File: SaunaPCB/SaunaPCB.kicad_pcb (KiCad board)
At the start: 2 copper layers, 200 x 110 mm, 61 parts, among them J201 KL3RM7.62, J202 KL3RM7.62, J203 KL3RM7.62, J204 KL2RM5.08, J205 KL3RM7.62, J206 KL3RM7.62, J301 KL2RM5.08, J302 KL2RM5.08, J303 KL2RM5.08, K201 Relais_SPDT_CO, K202 Relais_SPDT_CO, K203 Relais_SPDT_CO, K204 Relais_SPDT_CO, K205 Relais_SPDT_CO, K206 Relais_SPDT_CO, K207 Relais_SPDT_CO, U201 LHE05-20B24, U202 4N25, U203 4N25, U204 4N25, U301 ESP32-DEVKITC

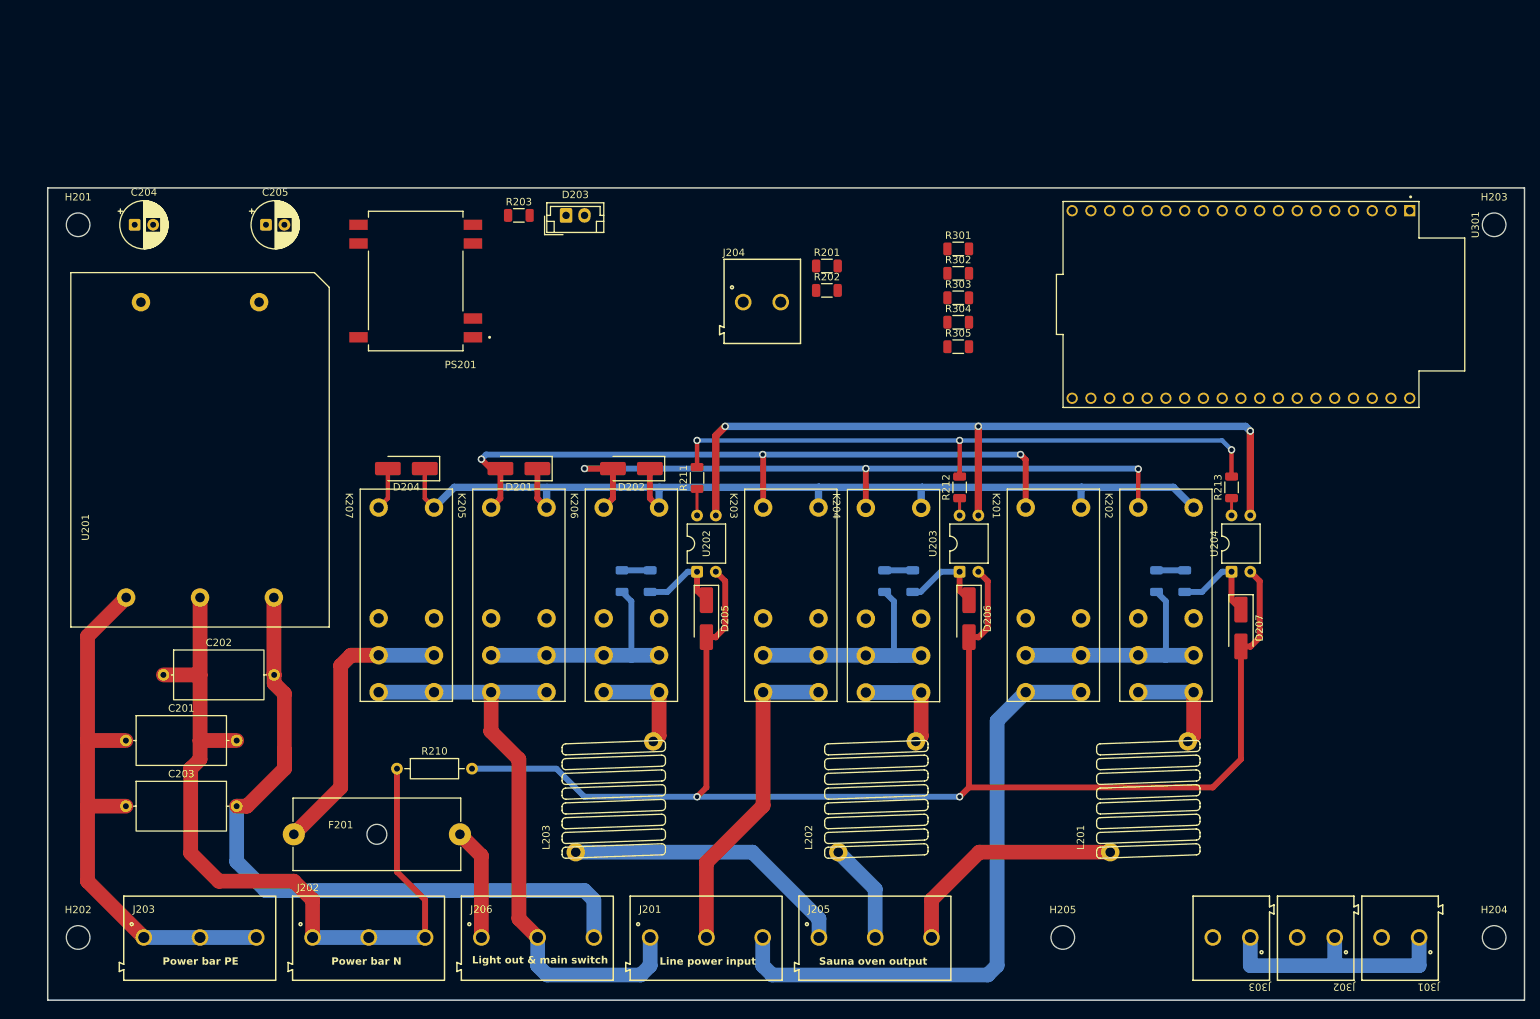
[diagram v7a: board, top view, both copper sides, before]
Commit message: 5V regulator changed
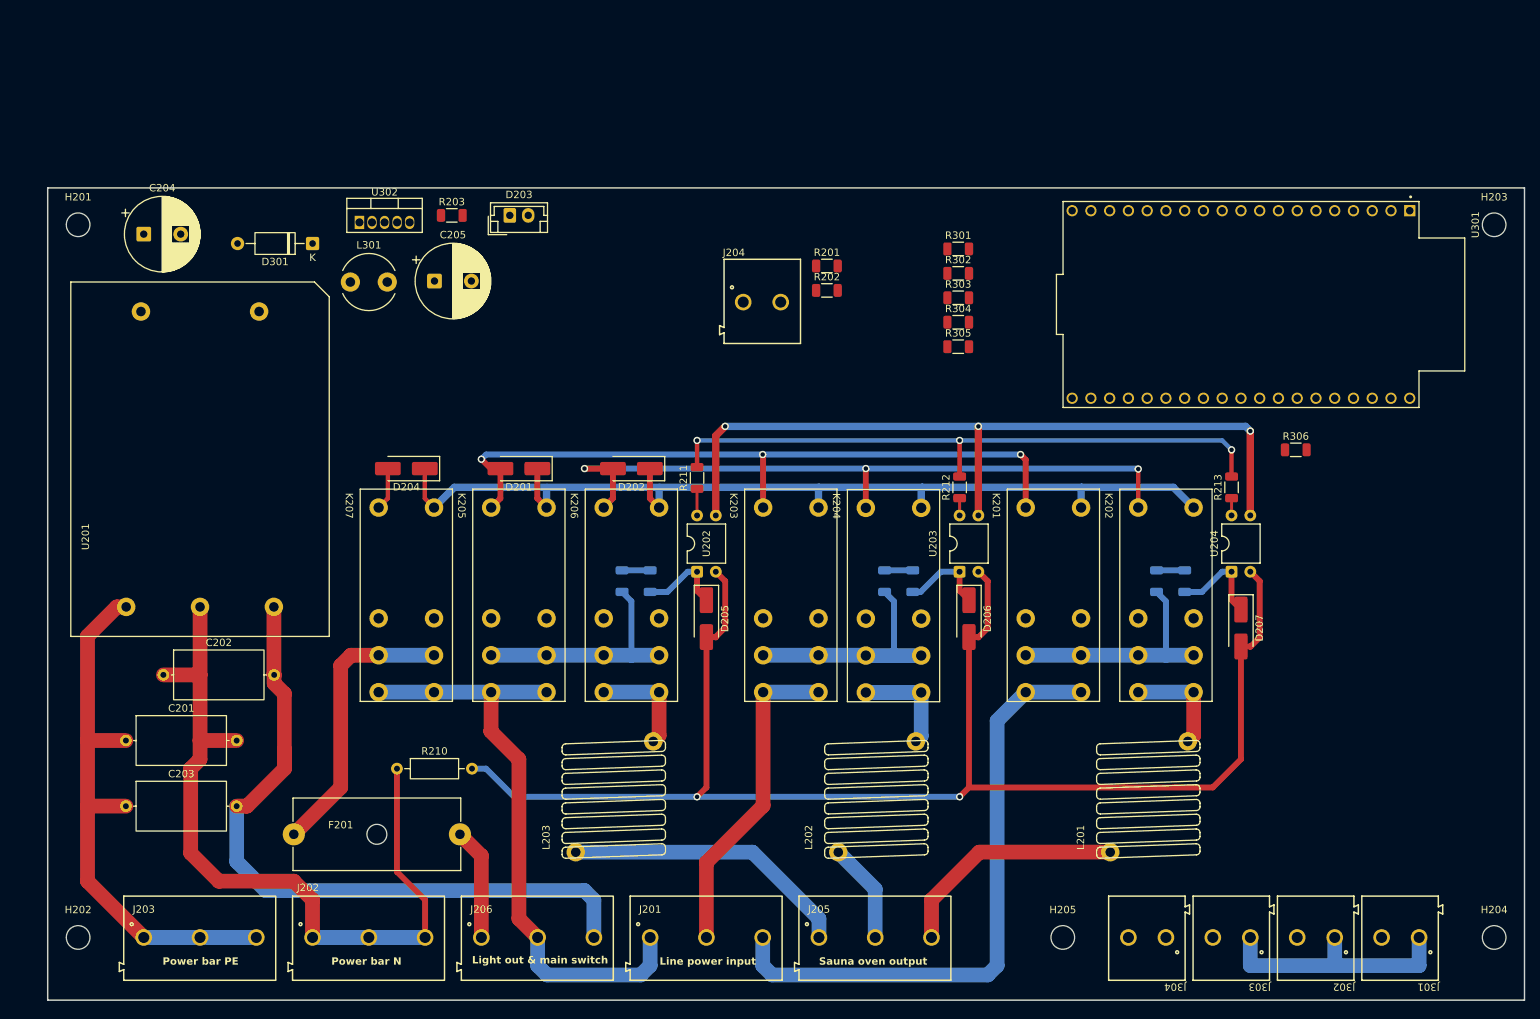
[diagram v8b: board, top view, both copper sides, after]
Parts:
- removed PS201: RSH2-2405S_H3-R, DCDC:CONV_RSH2-2405S_H3-R
- added D301: SB240, Diode_THT:D_A-405_P10.16mm_Horizontal, F.Cu at (102.9, 49.5)
- added J304: KL2RM5.08, MyConnectors:Terminal_Block_2_RM5.08, F.Cu at (215.9, 143.5)
- added L301: 100µH, Inductor_THT:L_Radial_D7.5mm_P5.00mm_Fastron_07P, F.Cu at (108.0, 54.7)
- added R306: 2K 1%, Resistor_SMD:R_1206_3216Metric, F.Cu at (236.0, 77.5)
- added U302: LM2576T-5, Package_TO_SOT_THT:TO-220-5_Vertical, F.Cu at (109.2, 46.7)
- C204: value 10µF/50V -> 100µF/63V 105°C Low ESR; footprint Capacitor_THT:CP_Radial_D6.3mm_P2.50mm -> Capacitor_THT:CP_Radial_D10.0mm_P5.00mm
- C205: value 10µF/50V -> 1000µF/16V 105°C Low ESR; footprint Capacitor_THT:CP_Radial_D6.3mm_P2.50mm -> Capacitor_THT:CP_Radial_D10.0mm_P5.00mm
- moved C205 24.1 mm to (119.4, 54.6)
- moved R203 9.08 mm to (121.7, 45.7)
- moved D203 7.62 mm to (129.6, 45.7)
- moved C204 1.77 mm to (80.0, 48.3)
- moved U201 1.27 mm to (87.6, 78.7)
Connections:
- U301 pad 16: Door_Contact -> unconnected-(U301-SD2-Pad16)
- U301 pad 23: unconnected-(U301-IO15-Pad23) -> Door_Contact
- U301 pad 26: unconnected-(U301-IO4-Pad26) -> KTY_Sensor
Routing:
- net L1_ON: track 98.0 -> 96.7 mm
- net N: track 109.0 -> 107.7 mm
- net PE: track 77.0 -> 76.5 mm
